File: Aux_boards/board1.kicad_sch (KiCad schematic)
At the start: 8 parts, among them J1 DB25_Receptacle_MountingHoles, J4 DC37_Plug_MountingHoles, U2 AMS1117-3.3

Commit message: db
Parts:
- added C3: 47 uF, symbol Device:C
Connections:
- net +24V: now also U1.1 (Vin+), U1.2 (Vin+)
- net GND: now also R1.2, U1.3 (Vin-), U1.4 (Vin-), U1.5 (Vout-), U1.6 (Vout-), C3.2
- net +5V: now reaches C1.1, U2.3 (VI)
- net +5V: now also D1.2 (A), U1.7 (Vout+), U1.8 (Vout+), C3.1
- net +3.3V: now reaches C2.1, U2.2 (VO)
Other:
- moved on the sheet: C1, C2, D1, R1, U1, U2

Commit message: worked on auxboard_1
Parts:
- added J2: DA15_Receptacle_MountingHoles, symbol Connector:DA15_Receptacle_MountingHoles
- added R10, R8: 220R, symbol Device:R
- added R11, R9: 10R, symbol Device:R
- added R12: 100R, symbol Device:R
- added R2, R5: 1k2, symbol Device:R
- added R3, R6: 180R, symbol Device:R
- added R4, R7: 33R, symbol Device:R
- added U3, U4, U5, U6, U7: SFH6345, SFH6345:SFH6345, symbol SFH6345:SFH6345
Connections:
- net +24V: now also J1.13, J1.25 (P25), J2.15 (P15), J2.8, U3.8, U4.8, U5.8, U6.8, U7.8
- net Alpha_ENC_A: now also J1.3
- net Alpha_LIM_1: now also J1.6
- net Beta_ENC_A: now also J1.4
- net Beta_LIM_1: now also J1.7
- net GND: now also J1.0 (PAD), J1.11, J1.15 (P15), J1.18 (P18), J1.2, J1.21 (P21), J1.5, J1.8, J2.0 (PAD), J2.10 (P10), J2.12 (P12), J2.14 (P14), J2.2, J2.4, J2.6, R11.2, R12.2, R4.1, R7.2, R9.2, U3.5, U4.5, U5.5, U6.5, U7.5
- net Theta_ENC_A: now also J1.1
- net Theta_LIM_CCW: now also J1.9
- net R_LIM_MIN: now reaches J1.10
- net R-Pos: now reaches J1.12
- net Theta_ENC_B: now reaches J1.14 (P14)
- net Alpha_ENC_B: now reaches J1.16 (P16)
- net Beta_ENC_B: now reaches J1.17 (P17)
- net Alpha_LIM_2: now reaches J1.19 (P19)
- net Beta_LIM_2: now reaches J1.20 (P20)
- net Theta_LIM_CLW: now reaches J1.22 (P22)
- net R_LIM_MAX: now reaches J1.23 (P23)
- net Theta_Pos: now reaches J1.24 (P24)
- net ALF_ENC_A_24 renamed Alpha_ENC_A_24
- net ALF_ENC_B_24 renamed Alpha_ENC_B_24
- net ALF_LIM_L_24 renamed Alpha_LIM_1_24
- net ALF_LIM_R_24 renamed Alpha_LIM_2_24
- net BET_ENC_A_24 renamed Beta_ENC_A_24
- net BET_ENC_B_24 renamed Beta_ENC_B_24
- net BET_LIM_DOWN_24 renamed Beta_LIM_2_24
- net BET_LIM_UP_24 renamed Beta_LIM_1_24
- net PHI_ENC_A_24 renamed Phi_ENC_A_24
- net Phi_ENC_A_24: now also U3.6
- net PHI_ENC_B_24 renamed Phi_ENC_B_24
- net Phi_ENC_B_24: now also U4.6
- net PHI_G_L_24 renamed Phi_Pos_24
- net Phi_Pos_24: now also U7.6
- net PHI_LIM_L_24 renamed Phi_LIM_CLW_24
- net Phi_LIM_CLW_24: now also U5.6
- net PHI_LIM_R_24 renamed Phi_LIM_CCW_24
- net Phi_LIM_CCW_24: now also U6.6
- net R_G_IN_24 renamed R_Pos_24
- net R_LIM_IN_24 renamed R_LIM_MAX_24
- net R_LIM_OUT_24 renamed R_LIM_MIN_24
- net TH_ENC_A_24 renamed Theta_ENC_A_24
- net TH_ENC_B_24 renamed Theta_ENC_B_24
- net TH_G_L_24 renamed Theta_Pos_24
- net TH_LIM_CCW_24 renamed Theta_LIM_CLW_24
- net TH_LIM_CLW_24 renamed Theta_LIM_CCW_24
- net Z_G_BOT_24 renamed Z_Pos_24
- net Z_LIM_BOT_24 renamed Z_LIM_DN_24
- net Z_LIM_TOP_24 renamed Z_LIM_UP_24
- new net: R5.1, R6.1
- new net: R5.2, U4.3
- new net: R2.1, R3.2
- new net: R2.2, U3.3
- new net: R10.1, R11.1
- new net: R10.2, U6.3
- new net: R12.1, U7.3
- new net: R6.2, R7.1
- new net: R8.1, R9.1
- new net: R3.1, R4.2
- new net: R8.2, U5.3
- new net Phi_ENC_A: U3.2
- new net Phi_ENC_B: U4.2
- new net Phi_LIM_CCW: U6.2
- new net Phi_LIM_CLW: U5.2
- new net Phi_Pos: U7.2
- new net R_ENC_A: J2.3
- new net R_ENC_B: J2.11 (P111)
- new net Z_ENC_A: J2.1
- new net Z_ENC_B: J2.9 (P9)
- new net Z_LIM_DN: J2.13 (P13)
- new net Z_LIM_UP: J2.5
- new net Z_Pos: J2.7
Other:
- moved on the sheet: C1, C2, C3, D1, J1, J4, R1, U1, U2

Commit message: dev
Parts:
- removed R10, R8: 220R, symbol Device:R
- added D2, D3: LED, symbol Device:LED
- added R11, R14, R17, R19, R7: 100k, symbol Device:R
- added R2, R3: R, symbol Device:R
- R13: renamed from R9; value 10R -> 100R
- R16: renamed from R11; value 10R -> 100R
- renumbered R7 to R10, R12 to R18, R2 to R4, R3 to R5, R4 to R6, R5 to R8, R6 to R9
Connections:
- net Alpha_ENC_A is gone; now on net Alpha_ENC_A_24: J1.3
- net Alpha_ENC_B is gone; now on net Alpha_ENC_B_24: J1.16 (P16)
- net Alpha_LIM_1 is gone; now on net Alpha_LIM_1_24: J1.6
- net Alpha_LIM_2 is gone; now on net Alpha_LIM_2_24: J1.19 (P19)
- net Beta_ENC_A is gone; now on net Beta_ENC_A_24: J1.4
- net Beta_ENC_B is gone; now on net Beta_ENC_B_24: J1.17 (P17)
- net Beta_LIM_1 is gone; now on net Beta_LIM_1_24: J1.7
- net Beta_LIM_2 is gone; now on net Beta_LIM_2_24: J1.20 (P20)
- net R_ENC_A is gone; now on net R_ENC_A_24: J2.3
- net R_ENC_B is gone; now on net R_ENC_B_24: J2.11 (P111)
- net R_LIM_MAX is gone; now on net R_LIM_MAX_24: J1.23 (P23)
- net R_LIM_MIN is gone; now on net R_LIM_MIN_24: J1.10
- net Theta_ENC_A is gone; now on net Theta_ENC_A_24: J1.1
- net Theta_ENC_B is gone; now on net Theta_ENC_B_24: J1.14 (P14)
- net Theta_LIM_CCW is gone; now on net Theta_LIM_CCW_24: J1.9
- net Theta_LIM_CLW is gone; now on net Theta_LIM_CLW_24: J1.22 (P22)
- net Theta_Pos is gone; now on net Theta_Pos_24: J1.24 (P24)
- net Z_ENC_A is gone; now on net Z_ENC_A_24: J2.1
- net Z_ENC_B is gone; now on net Z_ENC_B_24: J2.9 (P9)
- net Z_LIM_DN is gone; now on net Z_LIM_DN_24: J2.13 (P13)
- net Z_LIM_UP is gone; now on net Z_LIM_UP_24: J2.5
- net Z_Pos is gone; now on net Z_Pos_24: J2.7
- net +24V: now also R1.1, R11.1, R14.1, R17.1, R19.1, R7.1
- net +3.3V: now also R3.1
- net +5V: now also R2.1; no longer D1.2 (A)
- net GND: now also D1.1 (K), D2.1 (K), D3.1 (K); no longer R1.2
- net Phi_ENC_A_24: now also R7.2
- net Phi_ENC_B_24: now also R11.2
- net Phi_LIM_CCW_24: now also R17.2
- net Phi_LIM_CLW_24: now also R14.2
- net Phi_Pos_24: now also R19.2
- net at R16.1: now also U6.3
- net at R13.1: now also U5.3
- net R-Pos renamed R-Pos_24
- new net: D1.2 (A), R1.2
- new net: D3.2 (A), R3.2
- new net: D2.2 (A), R2.2
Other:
- moved on the sheet: C3, R13, R16

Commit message: commit message
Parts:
- removed R13, R16: 100R, symbol Device:R
- added J6: Conn_01x04_Pin, symbol Connector:Conn_01x04_Pin
- added J7, J8, J9: Conn_01x03_Pin, symbol Connector:Conn_01x03_Pin
- added R100, R97: 10R, symbol Device:R
- added R101, R103, R104, R98: 0R, symbol Device:R
- added R102, R99: 220R, symbol Device:R
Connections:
- net +24V: now also J6.1 (Pin_1)
- net +3.3V: now also J9.1 (Pin_1)
- net +5V: now also J7.1 (Pin_1), J8.1 (Pin_1)
- net GND: now also J6.4 (Pin_4), J8.3 (Pin_3), J9.3 (Pin_3), R101.2, R104.2, R98.2; no longer R18.2
- net Phi_ENC_A: now also J6.2 (Pin_2)
- net Phi_ENC_B: now also J6.3 (Pin_3)
- net Phi_LIM_CCW: now also J7.2 (Pin_2)
- net Phi_LIM_CLW: now also J8.2 (Pin_2)
- net Phi_Pos: now also J9.2 (Pin_2)
- net at U6.3: now also R102.2
- net at U5.3: now also R99.2
- new net: R103.1, R18.2
- new net: R103.2, R104.1
- new net: R100.2, R101.1
- new net: R100.1, R102.1
- new net: R97.1, R99.1
- new net: R97.2, R98.1

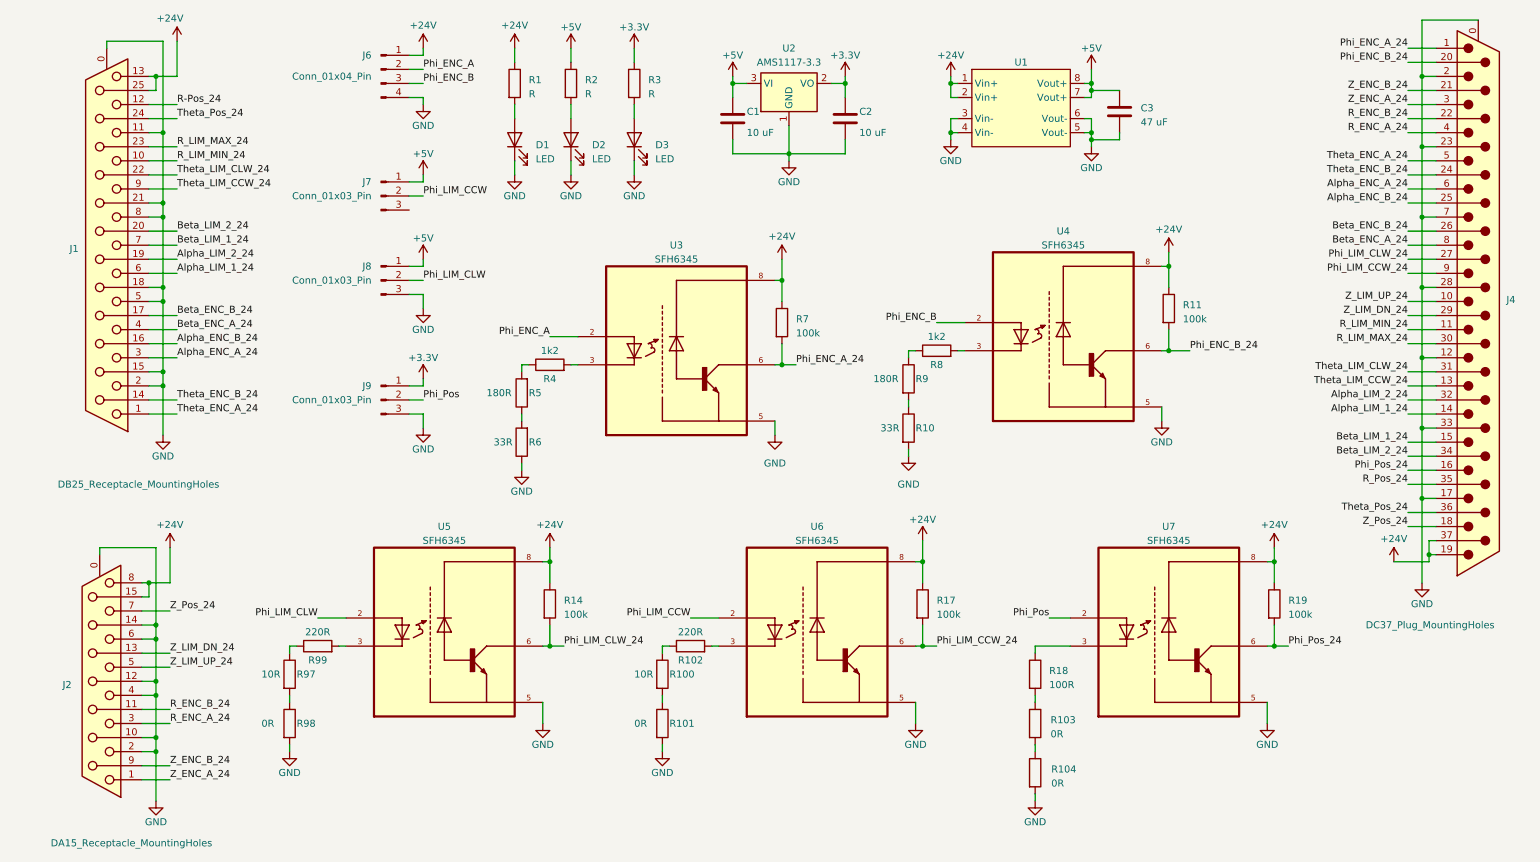
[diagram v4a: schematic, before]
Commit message: Removed unnecessary optocouplers
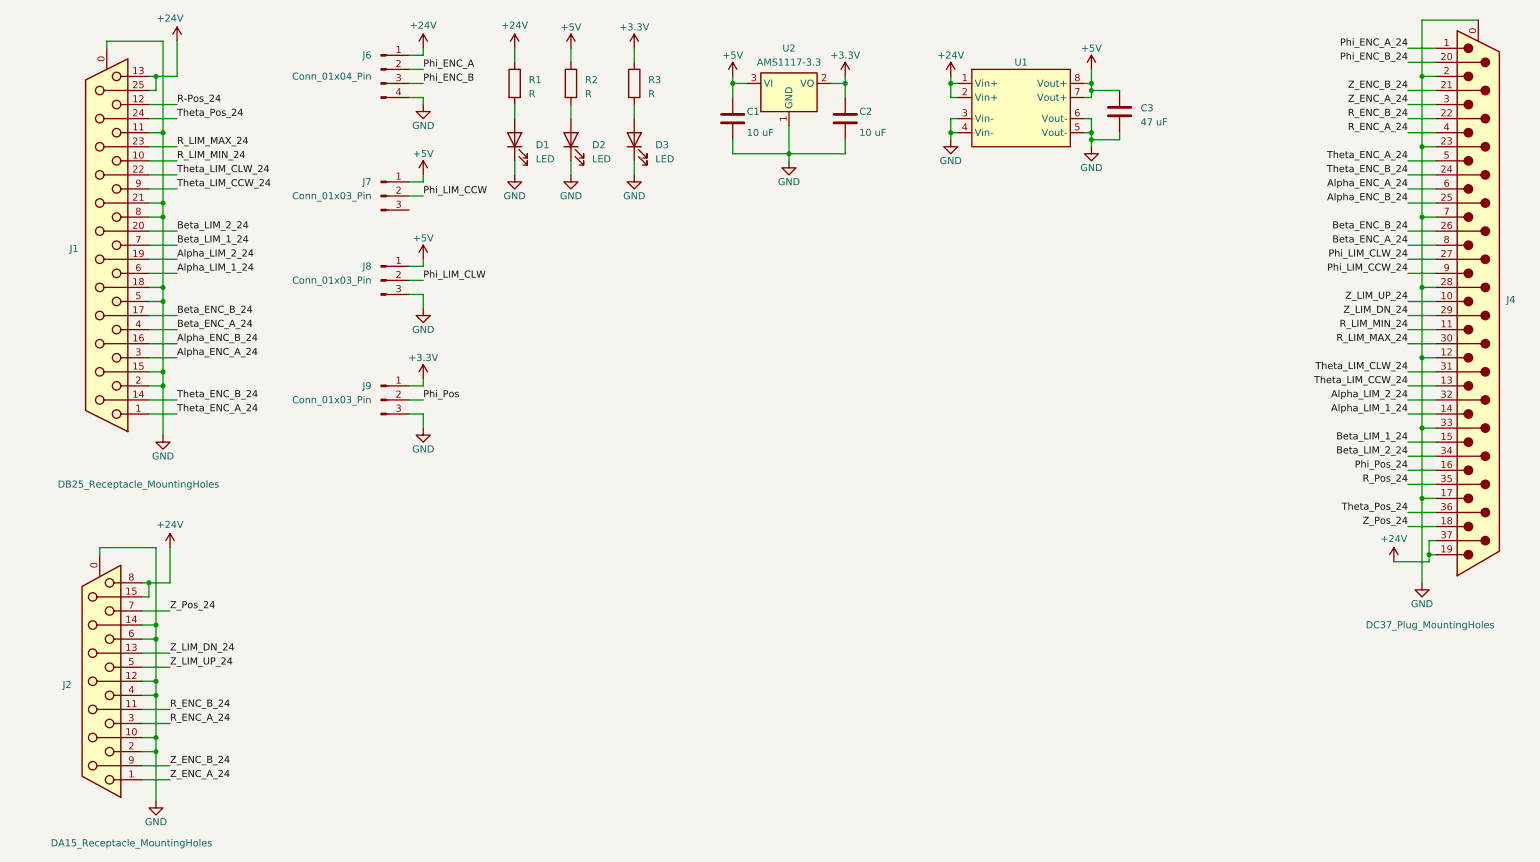
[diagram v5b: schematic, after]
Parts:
- removed R10, R6: 33R, symbol Device:R
- removed R100, R97: 10R, symbol Device:R
- removed R101, R103, R104, R98: 0R, symbol Device:R
- removed R102, R99: 220R, symbol Device:R
- removed R11, R14, R17, R19, R7: 100k, symbol Device:R
- removed R18: 100R, symbol Device:R
- removed R4, R8: 1k2, symbol Device:R
- removed R5, R9: 180R, symbol Device:R
- removed U3, U4, U5, U6, U7: SFH6345, SFH6345:SFH6345, symbol SFH6345:SFH6345
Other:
- company: (none) -> LEGO Kör (legokor.hu)
- title: (none) -> Karcsi (INDACT Robot Arm) - Auxiliary board 1
